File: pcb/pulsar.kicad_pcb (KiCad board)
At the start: 2 copper layers, 104.1 x 211.5 mm, 77 parts, among them J1 Conn_01x04, K1 KEYSW, K2 KEYSW, K3 KEYSW, K4 KEYSW, K5 KEYSW, K6 KEYSW, K7 KEYSW, K8 KEYSW, K9 KEYSW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

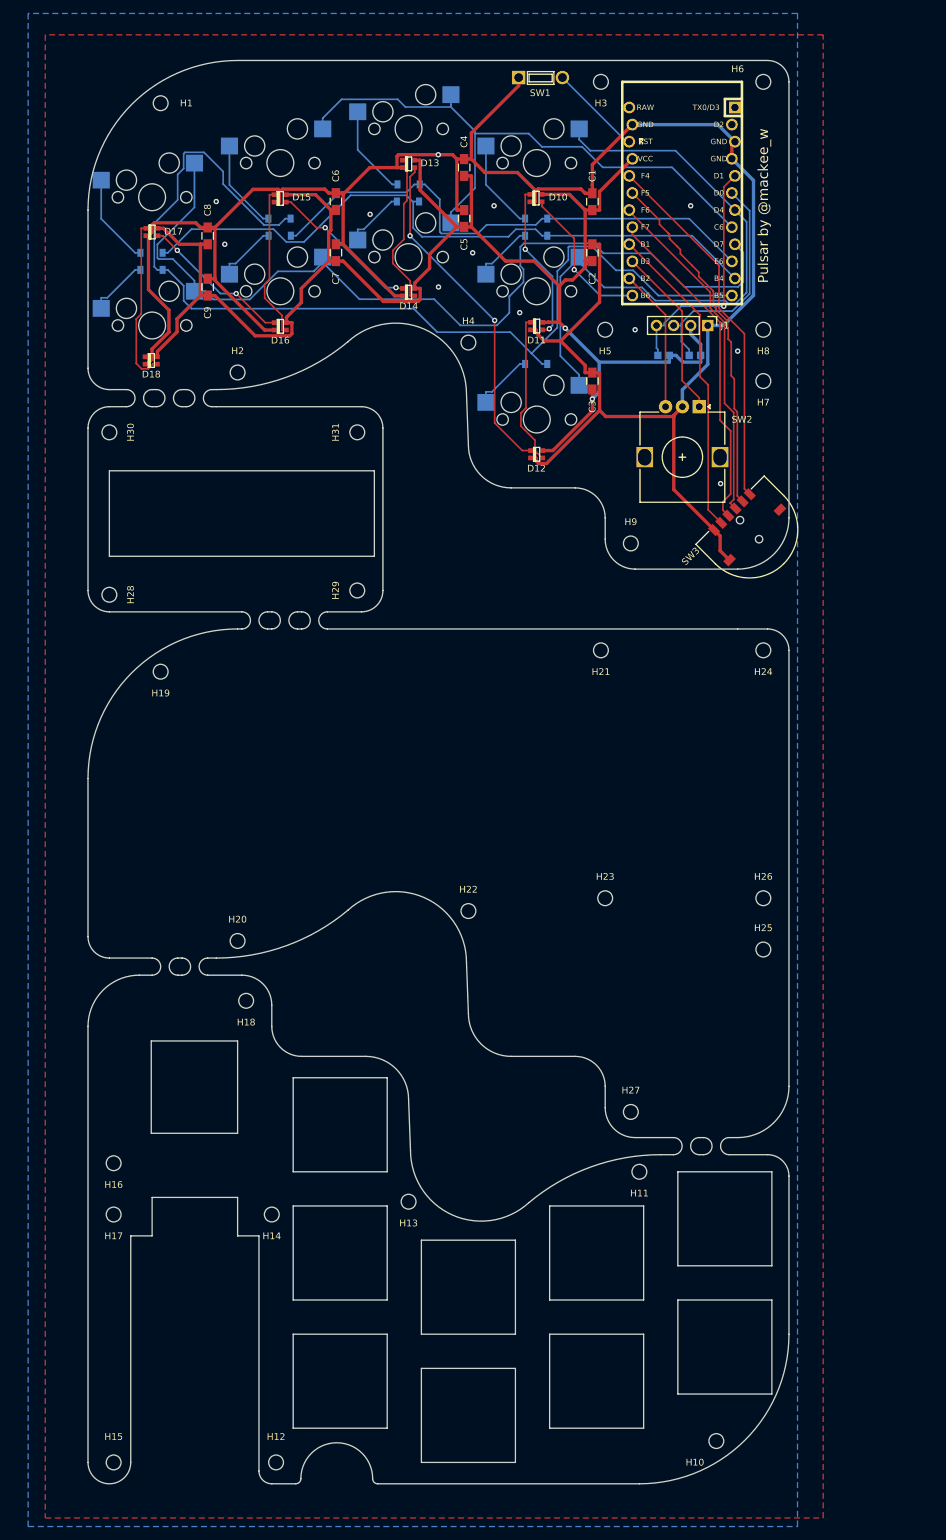
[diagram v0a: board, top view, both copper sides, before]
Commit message: update pcb: rev2.0 - 11 keys
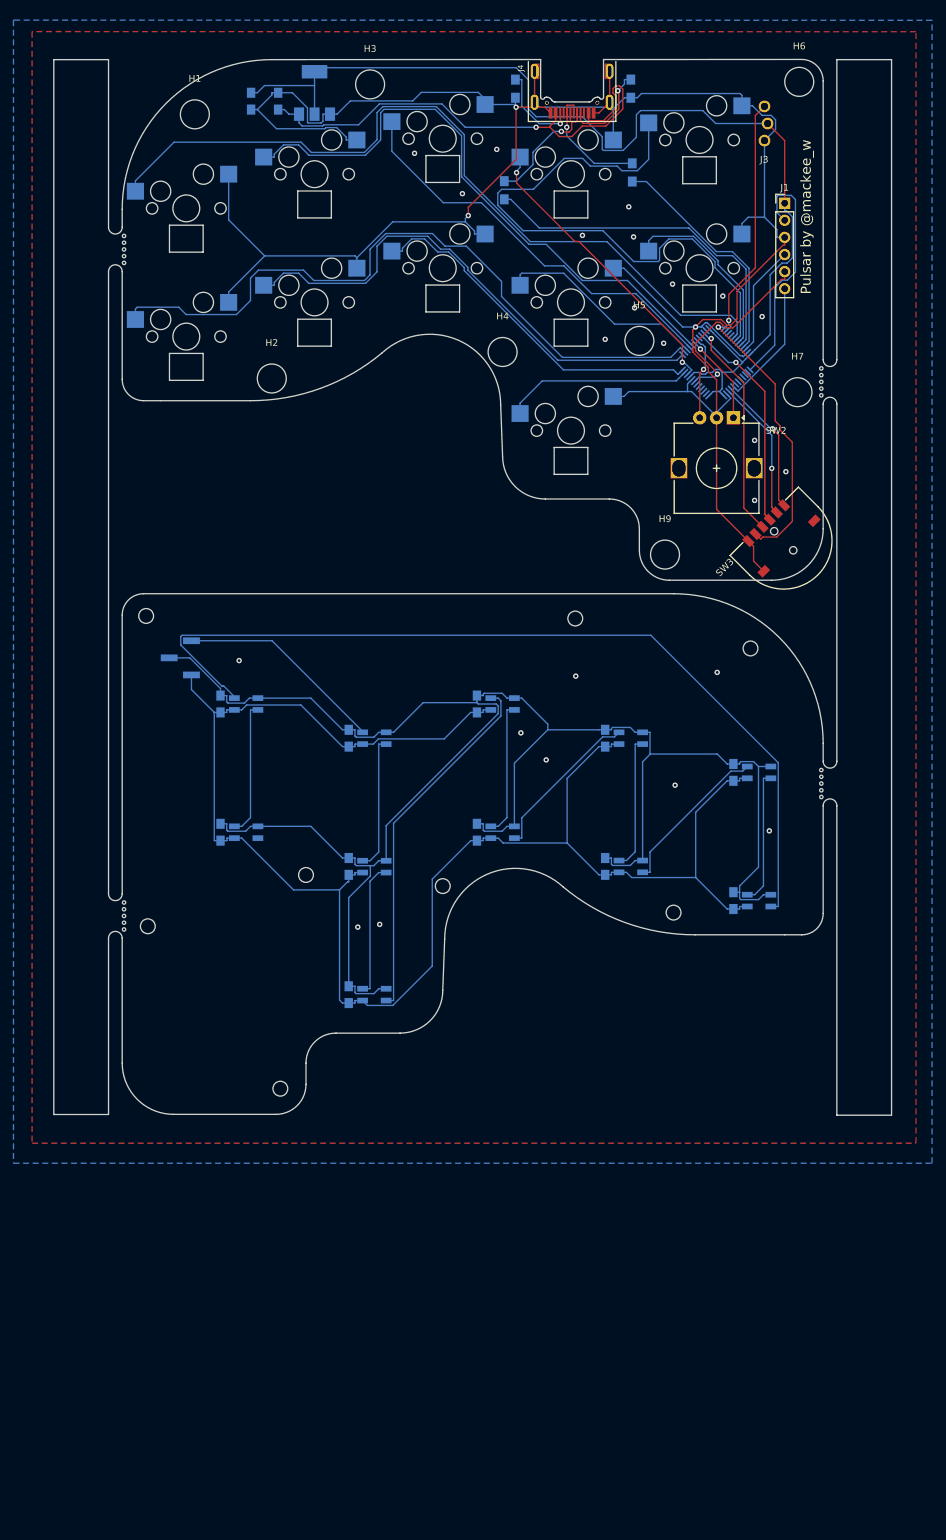
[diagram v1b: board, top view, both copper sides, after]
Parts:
- removed D12, D13, D14, D15, D16, D17, D18: WS2812B, WS2812-2020:WS2812B-2020
- removed G*** (x3): LOGO, pulsar:logosmall
- removed H17, H18, H19, H20, H21, H22, H23, H24, H25, H26, H27, H28, H29, H30, H31: MountingHole, Mounting_Holes:MountingHole_2.2mm_M2
- removed SW1: SW_PUSH, pluser:tactswitch-2lead-6mm
- added C10: 0.1u, Capacitors_SMD:C_0805_HandSoldering, B.Cu at (118.1, 161.6)
- added C11: 0.1u, Capacitors_SMD:C_0805_HandSoldering, B.Cu at (41.9, 132.4)
- added C12: 0.1u, Capacitors_SMD:C_0805_HandSoldering, B.Cu at (41.9, 151.5)
- added C13: 10uF, Capacitors_SMD:C_0805_HandSoldering, B.Cu at (50.5, 42.9)
- added J2: Conn_01x03, Pin_Headers:Pin_Header_Straight_1x03_Pitch2.54mm_SMD_Pin1Left, B.Cu at (35.9, 125.6)
- added J3: Conn_01x03, pulsar:3pin-zigzag, F.Cu at (122.7, 51.1)
- added J4: USB_C_Receptacle_USB2.0, usb-type-c:Mid_Mount-USB_C_HandSoldering, F.Cu at (94.1, 36.7)
- added K10: KEYSW, keyswitches:Kailh_socket, F.Cu at (113.1, 48.6)
- added K11: KEYSW, keyswitches:Kailh_socket, F.Cu at (113.1, 67.7)
- added R3: 22, Resistors_SMD:R_0805_HandSoldering, B.Cu at (103.1, 53.5)
- added R4: 22, Resistors_SMD:R_0805_HandSoldering, B.Cu at (84.1, 56.1)
- added U2: AMS1117-3.3, TO_SOT_Packages_SMD:SOT-223-3_TabPin2, B.Cu at (55.9, 41.7)
- C1: value 0.1u -> 22uF; moved to B.Cu
- C2, C3, C4, C5, C6, C7, C8, C9, H10, H11, H12, H13, H14, H15, H16, H8: moved to B.Cu
- D1, D2, D3, D4, D5, D6, D7, D8, D9: value D -> WS2812B; footprint Diodes_SMD:D_SOD-123 -> LED_SMD:LED_SK6812MINI_PLCC4_3.5x3.5mm_P1.75mm
- D10, D11: footprint WS2812-2020:WS2812B-2020 -> LED_SMD:LED_SK6812MINI_PLCC4_3.5x3.5mm_P1.75mm; moved to B.Cu
- H1, H2, H3, H4, H5, H6, H7, H9: footprint Mounting_Holes:MountingHole_2.2mm_M2 -> Mounting_Holes:MountingHole_4.3mm_M4
- J1: value Conn_01x04 -> Conn_01x06; footprint Pin_Headers:Pin_Header_Straight_1x04_Pitch2.54mm -> Pin_Headers:Pin_Header_Straight_1x06_Pitch2.54mm
- R1, R2: value R -> 5K1; footprint keyboard_parts:R_1608 -> Resistors_SMD:R_0805_HandSoldering
- U1: value ProMicro -> STM32F072C8Tx; footprint Keebio-Parts:ArduinoProMicro-ZigZag -> Housings_QFP:LQFP-48_7x7mm_Pitch0.5mm
- moved D9 130.1 mm to (121.9, 161.6)
- moved C4 124.1 mm to (61.0, 175.6), turned to 270 degrees
- moved D8 118.8 mm to (121.9, 142.6)
- moved C8 110.7 mm to (99.1, 156.6), turned to 270 degrees
- moved D7 107.2 mm to (102.9, 156.6)
- moved C9 106.3 mm to (118.1, 142.6), turned to 270 degrees
- moved D2 96.8 mm to (64.8, 156.6)
- moved D3 96.7 mm to (64.8, 175.6)
- moved C6 96.0 mm to (80.0, 151.5), turned to 270 degrees
- moved D5 94.7 mm to (83.8, 151.5)
- moved D6 93.2 mm to (102.9, 137.5)
- moved H14 90.9 mm to (30.9, 119.4)
- moved H12 89.1 mm to (74.9, 159.5)
- moved D11 86.7 mm to (45.7, 151.5)
- moved D10 86.6 mm to (45.7, 132.4)
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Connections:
- C2 pad 1: VCC -> +5V
- C3 pad 1: VCC -> +5V
- C4 pad 1: VCC -> +5V
- C5 pad 1: VCC -> +5V
- C6 pad 1: VCC -> +5V
- C7 pad 1: VCC -> +5V
- C8 pad 1: VCC -> +5V
- C9 pad 1: VCC -> +5V
- D1 pad 1: col1 -> +5V
- D10 pad 1: VCC -> +5V
- D10 pad 4: LEDD -> Net-(D10-Pad4)
- D11 pad 1: VCC -> +5V
- D11 pad 2: Net-(D11-Pad2) -> (no net)
- D2 pad 1: col2 -> +5V
- D3 pad 1: col3 -> +5V
- D4 pad 1: col1 -> +5V
- D5 pad 1: col2 -> +5V
- D6 pad 1: col3 -> +5V
- D7 pad 1: col1 -> +5V
- D8 pad 1: col2 -> +5V
- D9 pad 1: col3 -> +5V
- D9 pad 2: Net-(D9-Pad2) -> Net-(D10-Pad4)
- J1 pad 1: GND -> VCC
- J1 pad 2: VCC -> SWCLK
- J1 pad 3: SCL -> GND
- J1 pad 4: SDA -> SWDIO
- K1 pad 1: row1 -> GND
- K1 pad 2: Net-(D1-Pad2) -> sw1
- K2 pad 1: row1 -> GND
- K2 pad 2: Net-(D2-Pad2) -> sw6
- K3 pad 1: row1 -> GND
- K3 pad 2: Net-(D3-Pad2) -> sw2
- K4 pad 1: row2 -> GND
- K4 pad 2: Net-(D4-Pad2) -> sw7
- K5 pad 1: row2 -> GND
- K5 pad 2: Net-(D5-Pad2) -> sw3
- K6 pad 1: row2 -> GND
- K6 pad 2: Net-(D6-Pad2) -> sw8
- K7 pad 1: row3 -> GND
- K7 pad 2: Net-(D7-Pad2) -> sw4
- K8 pad 1: row3 -> GND
- K8 pad 2: Net-(D8-Pad2) -> sw9
- K9 pad 1: row3 -> GND
- K9 pad 2: Net-(D9-Pad2) -> sw5
- R1 pad 1: VCC -> Net-(J4-PadB5)
- R1 pad 2: SDA -> GND
- R2 pad 1: VCC -> Net-(J4-PadA5)
- R2 pad 2: SCL -> GND
- U1 pad 1: (no net) -> VCC
- U1 pad 10: col1 -> sw1
- U1 pad 11: col2 -> sw2
- U1 pad 12: col3 -> sw3
- U1 pad 13: LEDD -> sw4
- U1 pad 14: rotB -> sw5
- U1 pad 15: rotA -> sw6
- U1 pad 16: lev4 -> sw7
- U1 pad 17: lev3 -> sw8
- U1 pad 18: levT -> rotA
- U1 pad 19: lev2 -> rotB
- U1 pad 20: lev1 -> (no net)
- U1 pad 21: VCC -> levT
- U1 pad 22: Net-(SW1-Pad1) -> lev3
- U1 pad 24: (no net) -> VCC
- U1 pad 3: GND -> (no net)
- U1 pad 4: GND -> (no net)
- U1 pad 5: SDA -> (no net)
- U1 pad 6: SCL -> (no net)
- U1 pad 7: row1 -> NRST
- U1 pad 8: row2 -> GND
- U1 pad 9: row3 -> VCC
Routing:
- net +5V: track 0.00 -> 269.3 mm
- net GND: track 334.7 -> 592.1 mm, vias 12 -> 27
- net col3: track 151.6 -> 0.00 mm
- net row3: track 133.1 -> 0.00 mm
- net Net-(D10-Pad4): track 0.00 -> 131.8 mm
- net sw9: track 0.00 -> 118.6 mm
- net sw5: track 0.00 -> 104.0 mm
- net col2: track 99.3 -> 0.00 mm
- net row1: track 91.9 -> 0.00 mm
- net sw8: track 0.00 -> 88.6 mm
- net row2: track 88.2 -> 0.00 mm
- net sw10: track 0.00 -> 86.3 mm
- net col1: track 78.1 -> 0.00 mm
- net sw4: track 0.00 -> 77.2 mm
- net VCC: track 236.4 -> 160.7 mm, vias 2 -> 0
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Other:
- board size 104.1 x 211.5 mm -> 124.5 x 156.8 mm
- net class Default: trace_width 0.25 -> 0.2
- net class Power: trace_width 0.5 -> 0.2
